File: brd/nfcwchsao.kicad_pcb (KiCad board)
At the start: 2 copper layers, 34.3 x 48.3 mm, 13 parts, among them J1 Conn_02x03_Odd_Even, U1 NT3H2211, U2 CH32V003F4P6

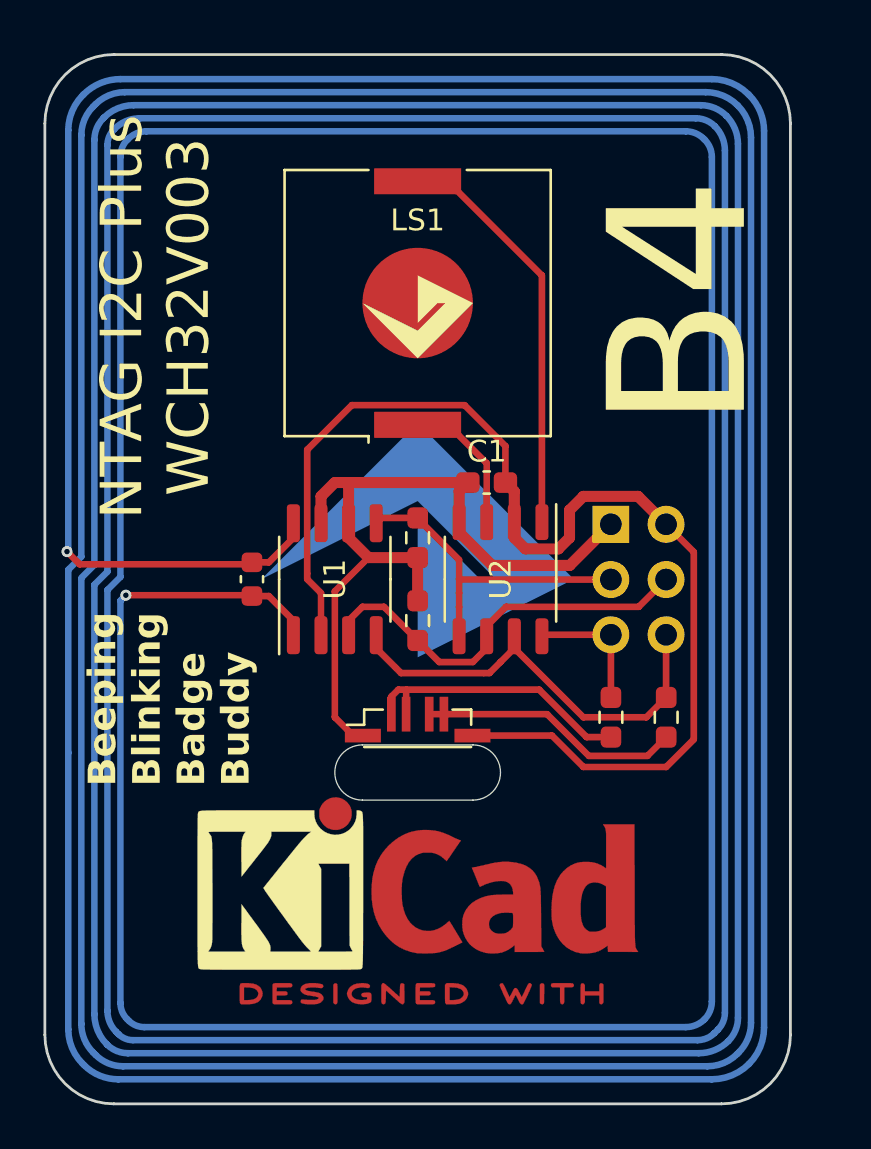
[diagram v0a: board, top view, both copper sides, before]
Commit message: updating to hand solder buzzer footprint, staggered header, single color LED
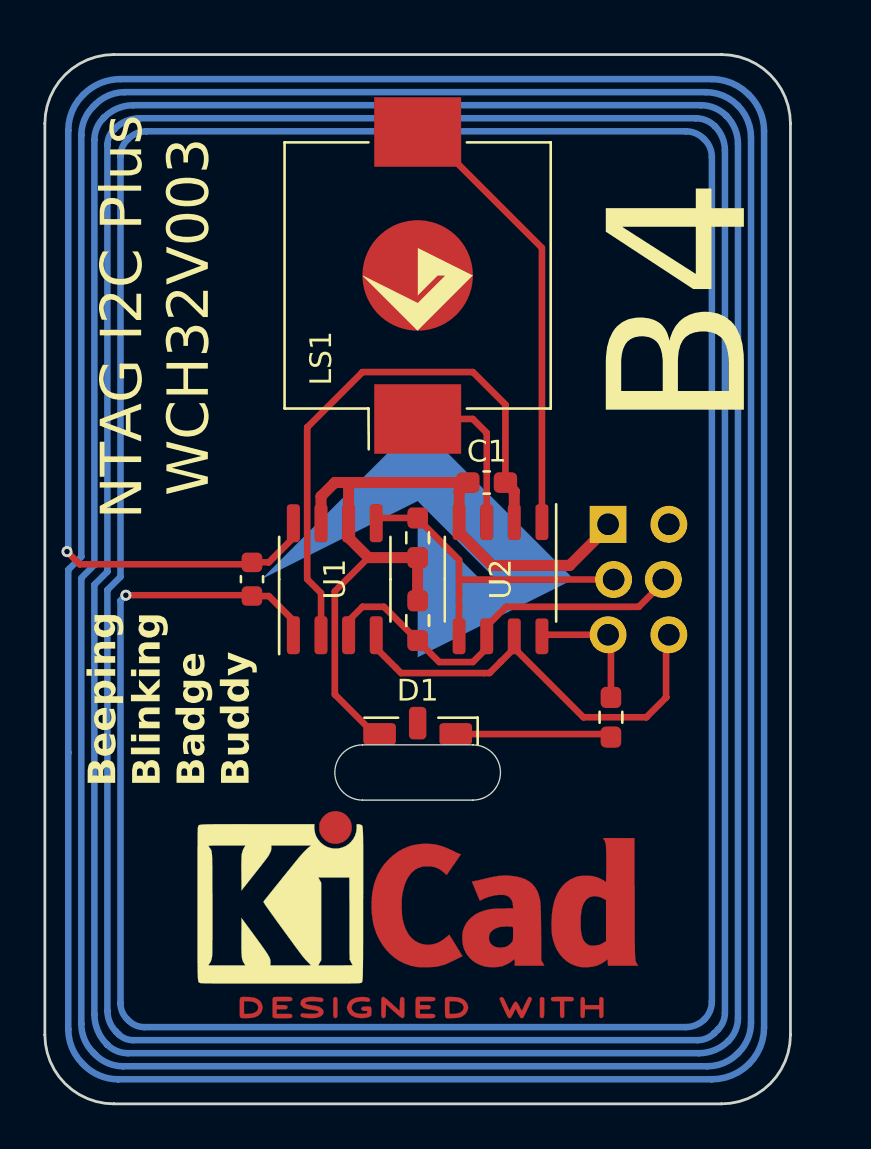
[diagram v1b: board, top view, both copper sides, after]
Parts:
- removed R2: 2k, Resistor_SMD:R_0603_1608Metric_Pad0.98x0.95mm_HandSolder
- D1: value LED_RGB -> Green; footprint custom:LED_Cree-PLCC6_4.7x1.5mm_extended pads -> custom:LED_Right_Angle_3x2x1mm
- J1: footprint Connector_PinHeader_2.54mm:PinHeader_2x03_P2.54mm_Vertical -> custom:PinHeader_2x03_P2.54mm_Staggered
- LS1: footprint Buzzer_Beeper:Buzzer_Murata_PKLCS1212E -> custom:Buzzer_Murata_PKLCS1212E_handy
- R1: value 1k -> 3.3k
- moved GS1 1.27 mm to (159.4, 87.6)
- moved LS1 1.27 mm to (159.4, 87.6)
- moved D1 0.76 mm to (159.4, 109.2), turned to 180 degrees
- moved REF** 0.64 mm to (159.4, 116.2)
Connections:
- D1 pad 1: VDD -> Net-(D1-K)
- D1 pad 2: Net-(D1-BK) -> VDD
- D1 pad 3: Net-(D1-BK) -> (no net)
- R1 pad 1: Net-(D1-BK) -> Net-(D1-K)
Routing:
- net GND: track 55.1 -> 26.2 mm
- net Net-(D1-BK): track 13.1 -> 0.00 mm
- net Net-(D1-GA): track 12.1 -> 0.00 mm
- net Net-(D1-K): track 0.00 -> 7.20 mm
- net /PZ+: track 18.9 -> 20.5 mm
- net /PZ-: track 6.62 -> 7.55 mm

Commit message: refining updates
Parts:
- moved R1 3.24 mm to (165.1, 107.3)
- moved GS1 1.27 mm to (159.4, 88.9)
- moved LS1 1.27 mm to (159.4, 88.9), turned to 0 degrees
- moved REF** 0.64 mm to (159.4, 116.8)
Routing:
- net GND: track 26.2 -> 46.4 mm
- net /PZ+: track 20.5 -> 10.4 mm
- net /PZ-: track 7.55 -> 15.4 mm
- net Net-(D1-K): track 7.20 -> 4.17 mm
- net /SWIO: track 6.08 -> 5.25 mm
- net /FD: track 20.0 -> 19.4 mm
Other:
- outline, holes or cut-outs redrawn

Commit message: cleaned up BOM, changed KiCad logo to all silkscreen
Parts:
- removed the REF** at (159.4, 116.8)
- added REF**: KiCad-Logo2_8mm_SilkScreen, Symbol:KiCad-Logo2_8mm_SilkScreen, F.Cu at (159.4, 115.6)
- C1: value 1uF -> 4.7uF
